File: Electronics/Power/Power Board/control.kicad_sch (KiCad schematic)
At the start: 10 parts, among them IC1 STM32U575VGT6, IC2 TJA1057GT/3, J2 USB4056-03-A, J4 Screw_Terminal_01x02, J5 TC2030

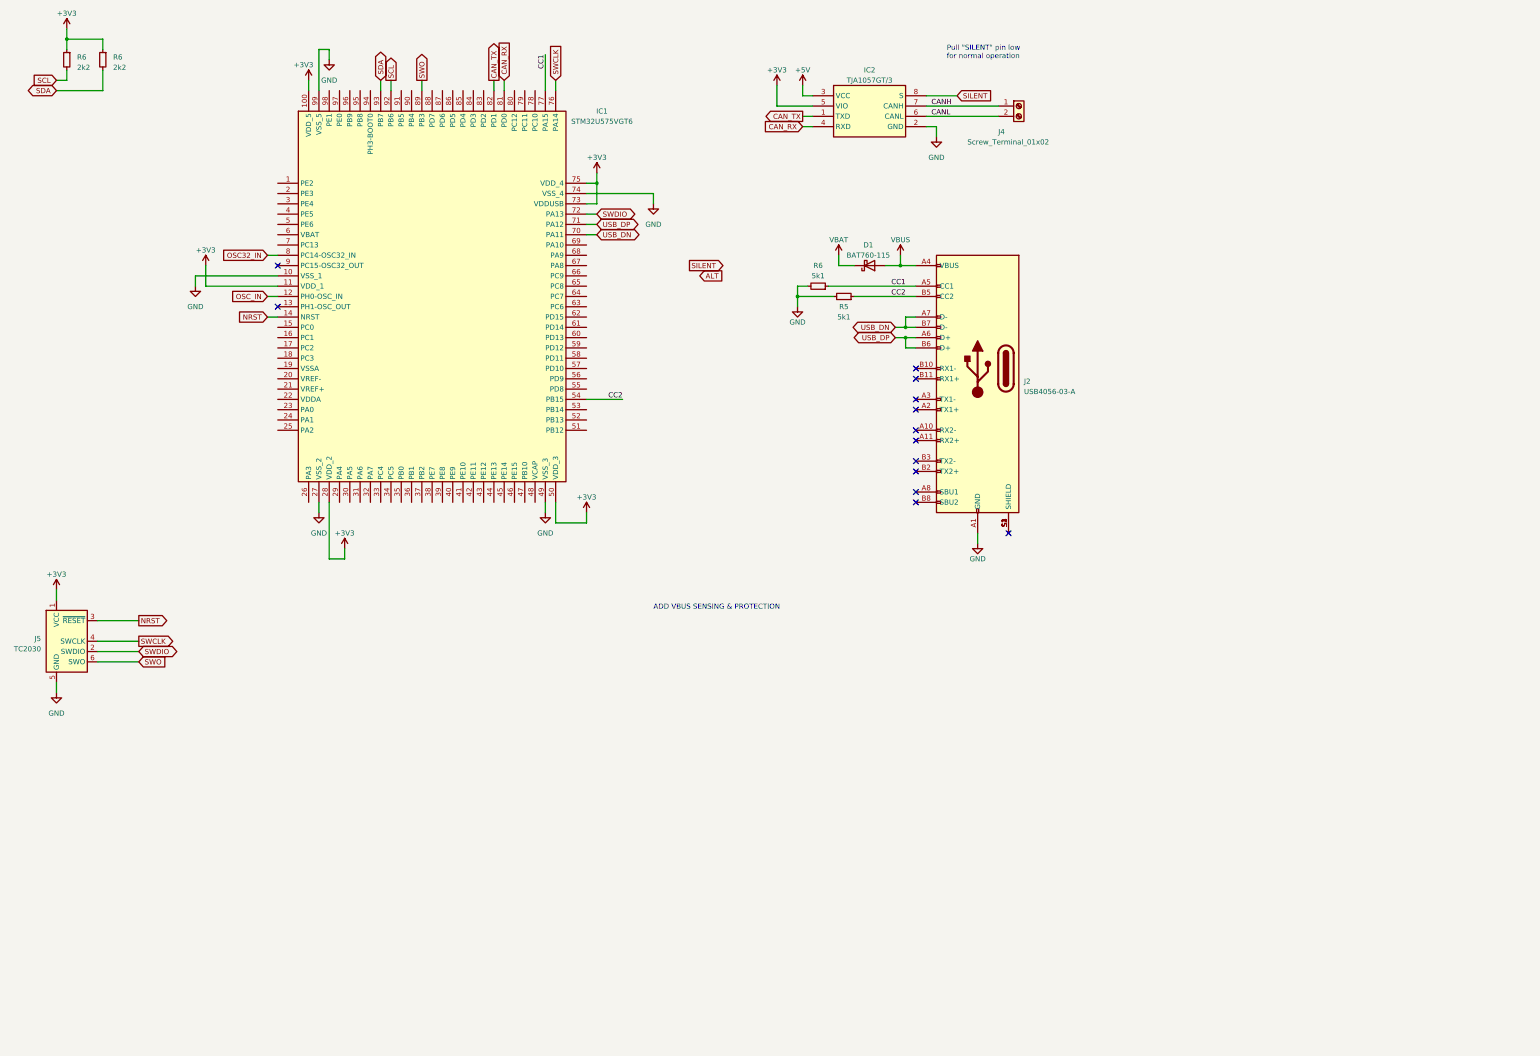
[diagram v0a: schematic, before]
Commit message: Motor driver + power board progress
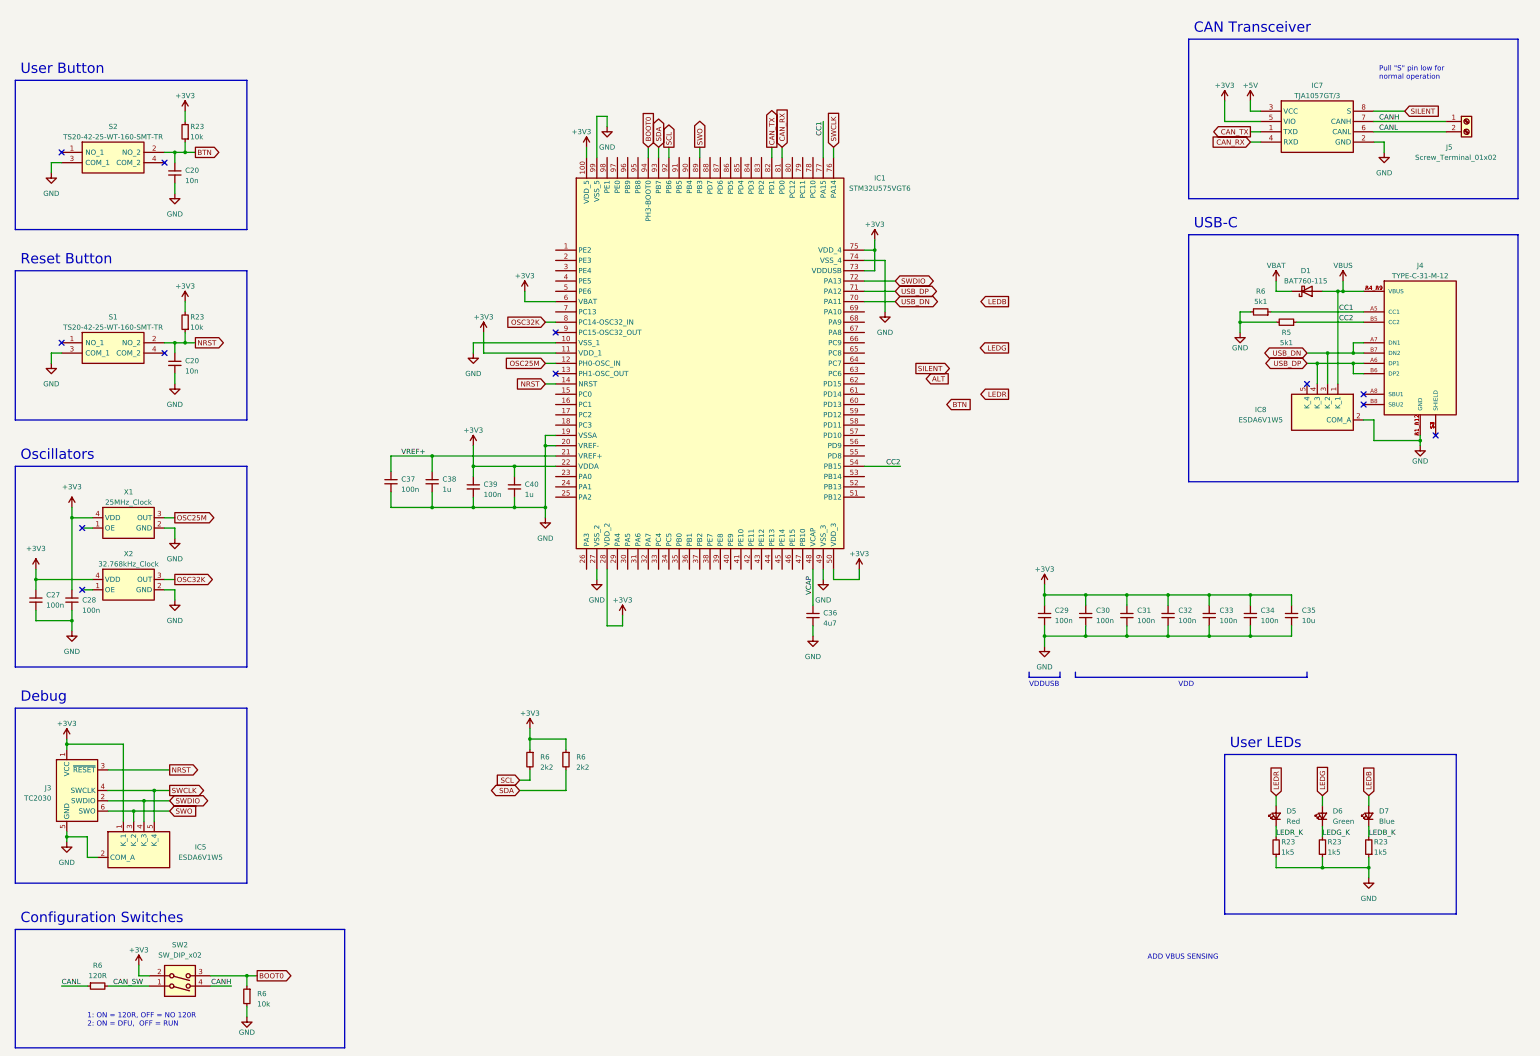
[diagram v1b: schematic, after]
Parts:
- removed J2: USB4056-03-A, MSL Footprints:USB405603A, symbol USB4056-03-A-MSL:USB4056-03-A
- added C20 (x2): 10n, Capacitor_SMD:C_0402_1005Metric, symbol Device:C_Small
- added C27, C28, C29, C30, C31, C32, C33, C34, C37, C39: 100n, Capacitor_SMD:C_0402_1005Metric, symbol Device:C_Small
- added C35: 10u, Capacitor_SMD:C_0402_1005Metric, symbol Device:C_Small
- added C36: 4u7, Capacitor_SMD:C_0402_1005Metric, symbol Device:C_Small
- added C38, C40: 1u, Capacitor_SMD:C_0402_1005Metric, symbol Device:C_Small
- added D5: Red, LED_SMD:LED_0603_1608Metric, symbol Device:LED_Small
- added D6: Green, LED_SMD:LED_0603_1608Metric, symbol Device:LED_Small
- added D7: Blue, LED_SMD:LED_0603_1608Metric, symbol Device:LED_Small
- added IC5, IC8: ESDA6V1W5, SOT65P210X110-5N, symbol ESDA6V1W5:ESDA6V1W5
- added J4: TYPE-C-31-M-12, MSL Footprints:HRO_TYPE-C-31-M-12, symbol TYPE-C-31-M-12:TYPE-C-31-M-12
- added R23 (x2), R6: 10k, Resistor_SMD:R_0402_1005Metric, symbol Device:R_Small
- added R23 (x3): 1k5, Resistor_SMD:R_0402_1005Metric, symbol Device:R_Small
- added R6: 120R, Resistor_SMD:R_0402_1005Metric, symbol Device:R_Small
- added S1, S2: TS20-42-25-WT-160-SMT-TR, MSL Footprints:TS204225WT160SMTTRMSL, symbol TS20-42-25-WT-160-SMT-TR-MSL:TS20-42-25-WT-160-SMT-TR
- added SW2: SW_DIP_x02, Package_DIP:DIP-4_W8.89mm_SMDSocket_LongPads, symbol Switch:SW_DIP_x02
- added X1: 25MHz_Clock, Oscillator:Oscillator_SMD_Abracon_ASE-4Pin_3.2x2.5mm_HandSoldering, symbol MSL_Symbols:25MHz_Clock
- added X2: 32.768kHz_Clock, Oscillator:Oscillator_SMD_Abracon_ASE-4Pin_3.2x2.5mm_HandSoldering, symbol MSL_Symbols:32.768kHz_Clock
- renumbered IC2 to IC7, J5 to J3, J4 to J5
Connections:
- net +3V3: now also IC1.22 (VDDA), IC1.6 (VBAT), C27.1, C28.2, C29.1, C30.1, C31.1, C32.1, C33.1, C34.1, C35.1, C39.1, C40.1, IC5.1 (K_1), R23.2, R23.2, SW2.2, X1.4 (VDD), X2.4 (VDD)
- net CANH: now also SW2.4
- net CANL: now also R6.1
- net CC1: now also J4.A5 (CC1)
- net CC2: now also J4.B5 (CC2)
- net GND: now also IC1.19 (VSSA), IC1.20 (VREF-), C20.2, C20.2, C27.2, C28.1, C29.2, C30.2, C31.2, C32.2, C33.2, C34.2, C35.2, C36.2, C37.2, C38.2, C39.2, C40.2, IC5.2 (COM_A), IC8.2 (COM_A), J4.A1_B12 (GND), J4.B1_A12 (GND), R23.1, R23.1, R23.1, R6.2, S1.3 (COM_1), S2.3 (COM_1), X1.2 (GND), X2.2 (GND)
- net NRST: now also C20.1, R23.1, S1.2 (NO_2)
- net SWCLK: now also IC5.5 (K_4)
- net SWDIO: now also IC5.4 (K_3)
- net SWO: now also IC5.3 (K_2)
- net USB_DN: now also IC8.3 (K_2), J4.A7 (DN1), J4.B7 (DN2)
- net USB_DP: now also IC8.4 (K_3), J4.A6 (DP1), J4.B6 (DP2)
- net VBUS: now also IC8.1 (K_1), J4.A4_B9 (VBUS), J4.B4_A9 (VBUS)
- net VREF+: now reaches IC1.21 (VREF+)
- net VREF+: now also C37.1, C38.1
- net VCAP: now reaches IC1.48 (VCAP)
- net VCAP: now also C36.1
- net BOOT0: now reaches IC1.94 (PH3-BOOT0)
- net BOOT0: now also R6.1, SW2.3
- net OSC32_IN renamed OSC32K
- net OSC32K: now also X2.3 (OUT)
- net OSC_IN renamed OSC25M
- net OSC25M: now also X1.3 (OUT)
- new net: J4.S1 (SHIELD), J4.S2 (SHIELD), J4.S3 (SHIELD), J4.S4 (SHIELD)
- new net BTN: C20.1, R23.1, S2.2 (NO_2)
- new net CAN_SW: R6.2, SW2.1
- new net LEDB: D7.2 (A)
- new net LEDB_K: D7.1 (K), R23.2
- new net LEDG: D6.2 (A)
- new net LEDG_K: D6.1 (K), R23.2
- new net LEDR: D5.2 (A)
- new net LEDR_K: D5.1 (K), R23.2
- no-connect marks 13 -> 12
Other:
- note added: "1: ON = 120R, OFF = NO 120R 2: ON = DFU, OFF = RUN"
- note added: "ADD VBUS SENSING"
- note added: "CAN Transceiver"
- note added: "Configuration Switches"
- note added: "Debug"
- note added: "Oscillators"
- note added: "Pull "S" pin low for normal operation"
- note added: "Reset Button"
- note added: "USB-C"
- note added: "User Button"
- note added: "User LEDs"
- note added: "VDD"
- note added: "VDDUSB"
- note removed: "ADD VBUS SENSING & PROTECTION"
- note removed: "Pull "SILENT" pin low for normal operation"
- moved on the sheet: D1, IC1, IC7, J3, J5, R5, R6

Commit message: PCB Schematic progress
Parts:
- removed IC5, IC8: ESDA6V1W5, SOT65P210X110-5N, symbol ESDA6V1W5:ESDA6V1W5
- removed J4: TYPE-C-31-M-12, MSL Footprints:HRO_TYPE-C-31-M-12, symbol TYPE-C-31-M-12:TYPE-C-31-M-12
- added J1: TYPE-C-31-M-12, MSL Footprints:HRO_TYPE-C-31-M-12, symbol TYPE-C-31-M-12:TYPE-C-31-M-12
- added U1, U2: USBLC6-4SC6-ES, Package_TO_SOT_SMD:SOT-23-6, symbol MSL_Symbols:USBLC6-4SC6-ES
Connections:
- net +3V3: now also U2.5 (VBUS)
- net CC1: now also J1.A5 (CC1), U1.1 (IO1)
- net CC2: now also J1.B5 (CC2), U1.3 (IO2)
- net GND: now also J1.A1_B12 (GND), J1.B1_A12 (GND), U1.2 (GND), U2.2 (GND)
- net NRST: now also U2.6 (IO4)
- net SWCLK: now also U2.4 (IO3)
- net SWDIO: now also U2.3 (IO2)
- net SWO: now also U2.1 (IO1)
- net USB_DN: now also J1.A7 (DN1), J1.B7 (DN2), U1.6 (IO4)
- net USB_DP: now also J1.A6 (DP1), J1.B6 (DP2), U1.4 (IO3)
- net VBUS: now also J1.A4_B9 (VBUS), J1.B4_A9 (VBUS), U1.5 (VBUS)
- net VBAT renamed VIN
- new net: J1.S1 (SHIELD), J1.S2 (SHIELD), J1.S3 (SHIELD), J1.S4 (SHIELD)
- no-connect marks 12 -> 11
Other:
- note added: "Decoupling Capacitors"
- note added: "I2C Pullups"
- moved on the sheet: C29, C30, C31, C32, C33, C34, C35, C36, C37, C38, C39, C40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

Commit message: PCB Schematics finished
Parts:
- renumbered C27 to C301, C28 to C302, C37 to C305, C38 to C306, C39 to C307, C40 to C308, C36 to C309, C29 to C310, C30 to C311, C31 to C312, C32 to C313, C33 to C314, C34 to C315, C35 to C316, IC7 to IC302, J5 to J303, S2 to S301, S1 to S302, SW2 to SW301, X1 to X301, X2 to X302
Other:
- moved on the sheet: R6

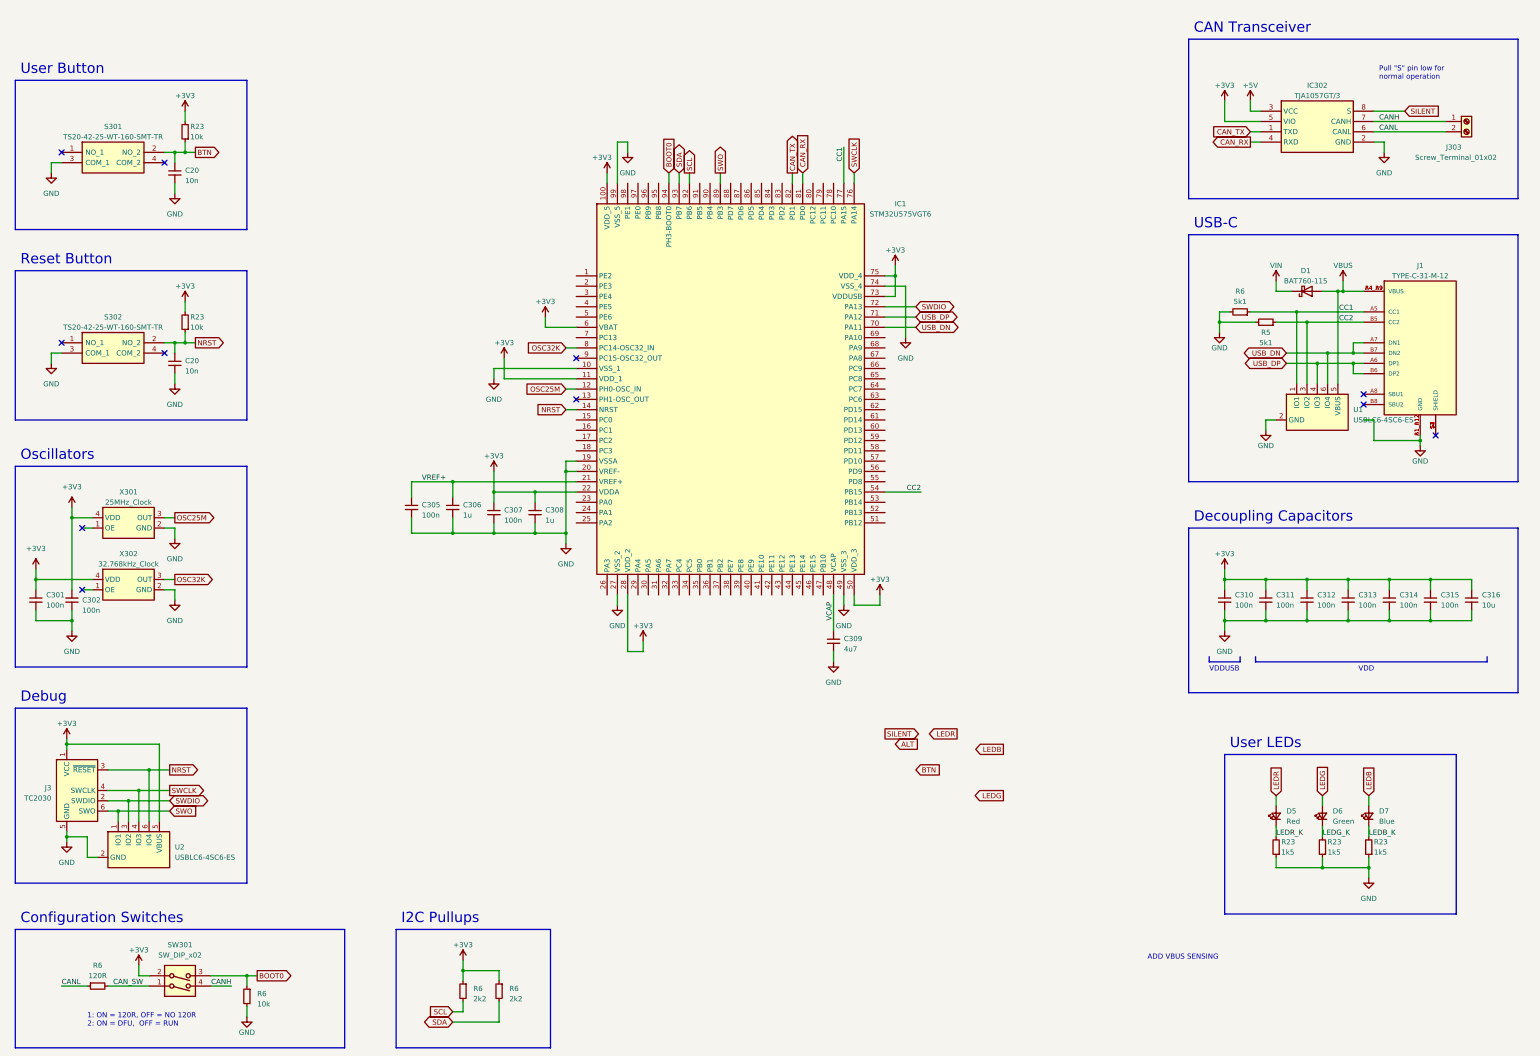
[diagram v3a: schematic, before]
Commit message: Schematic updates
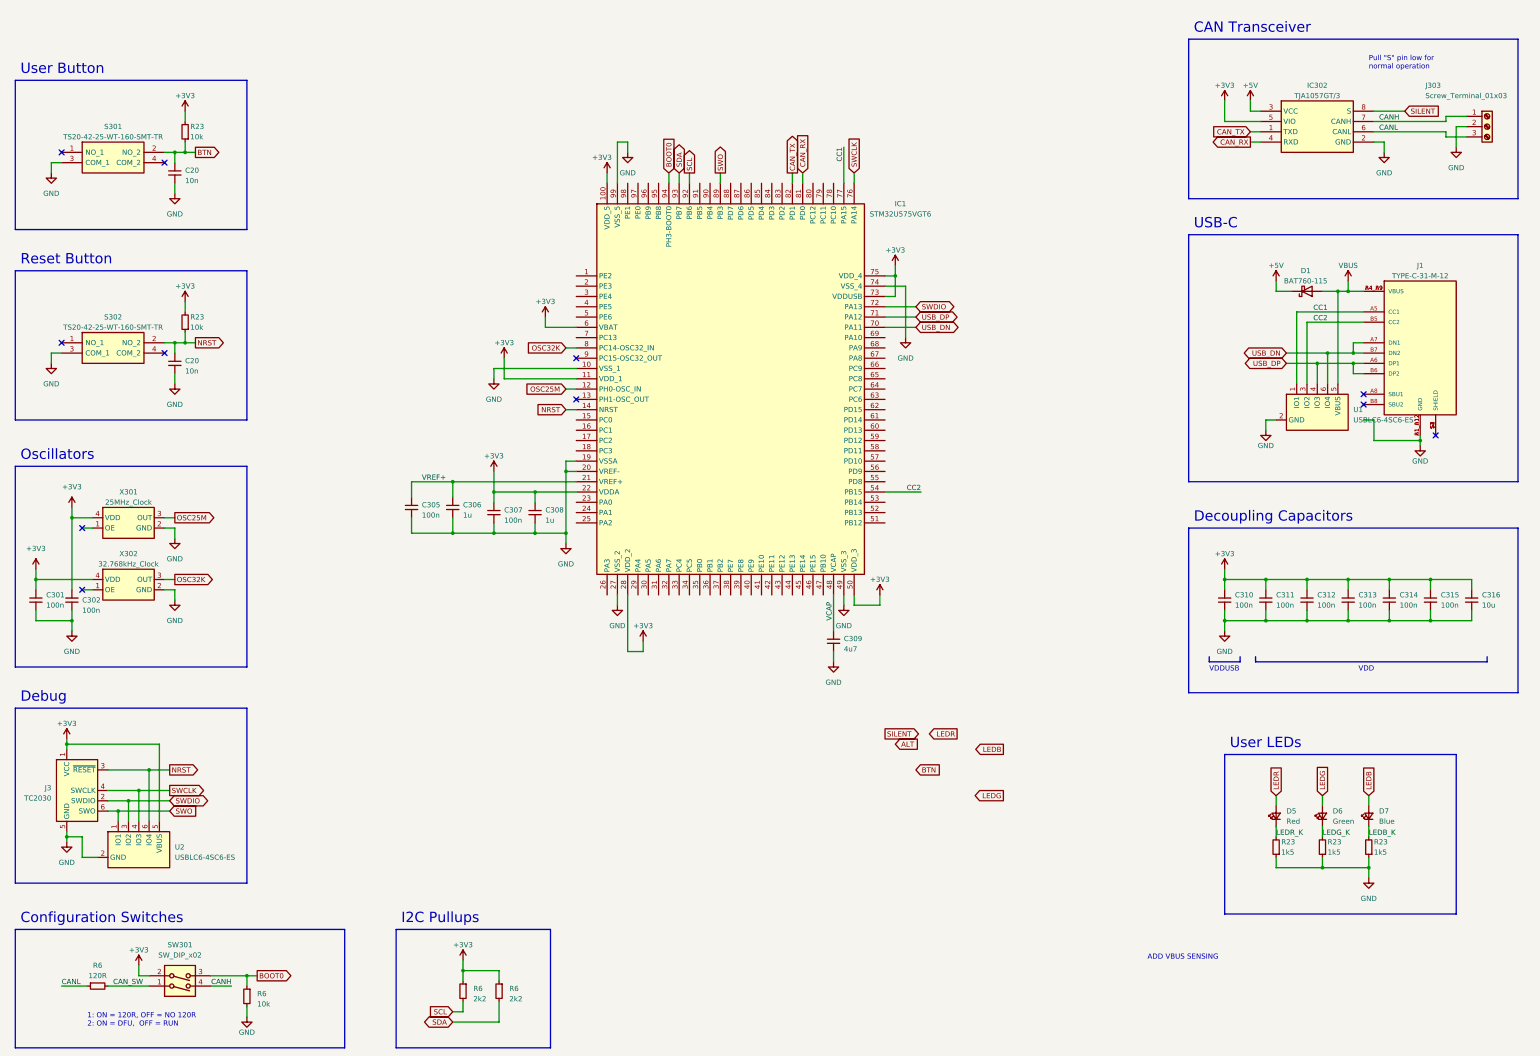
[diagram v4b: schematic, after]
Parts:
- removed J303: Screw_Terminal_01x02, TerminalBlock:TerminalBlock_bornier-2_P5.08mm, symbol Connector:Screw_Terminal_01x02
- removed R5, R6: 5k1, Resistor_SMD:R_0402_1005Metric, symbol Device:R_Small
- added J303: Screw_Terminal_01x03, TerminalBlock:TerminalBlock_bornier-3_P5.08mm, symbol Connector:Screw_Terminal_01x03
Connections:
- net VIN is gone; now on net +5V: D1.1 (K)
- net CANH: now also J303.1 (Pin_1)
- net CANL: now also J303.3 (Pin_3)
- net GND: now also J303.2 (Pin_2)

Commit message: PCB layout progress, spice simulations for power board
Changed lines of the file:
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@@
+    )
+  )
+  (global_label "12V_EN" (shape output) (at 256.54 193.04 180) (fields_autoplaced)
+    (effects (font (size 1.27 1.27)) (justify right))
+    (property "Intersheetrefs" "${INTERSHEET_REFS}" (at 246.6795 193.04 0)
+      (effects (font (size 1.27 1.27)) (justify right) hide)
     )
   )

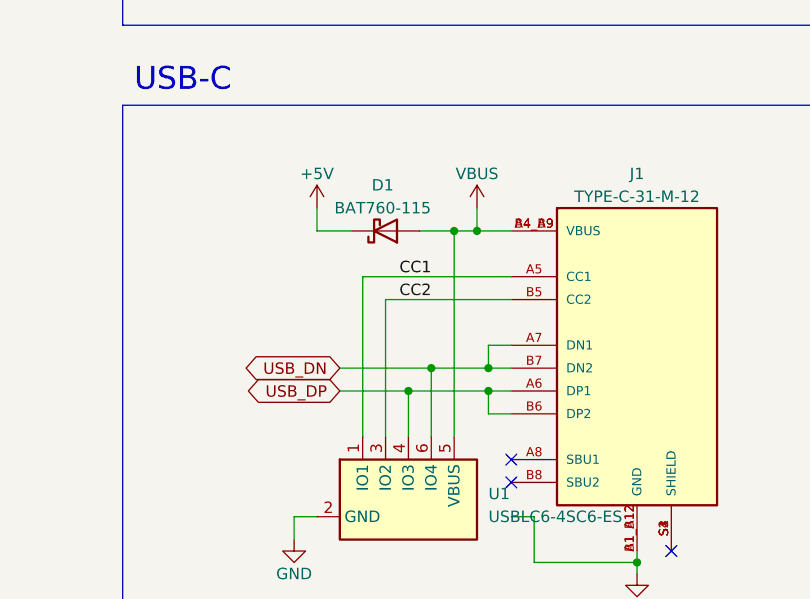
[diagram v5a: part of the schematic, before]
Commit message: Implemented power supply selector
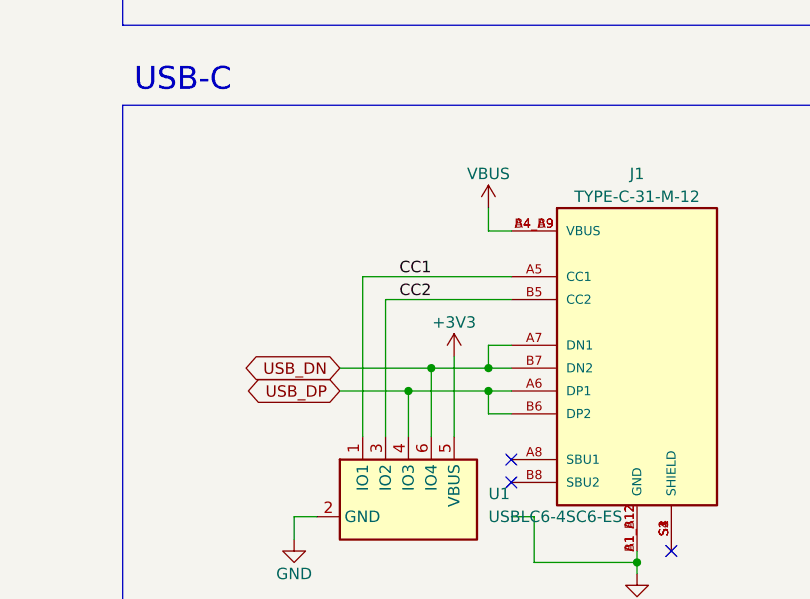
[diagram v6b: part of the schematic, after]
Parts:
- removed D1: BAT760-115, Diode_SMD:D_SOD-323, symbol Device:D_Schottky
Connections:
- net +3V3: now also U1.5 (VBUS)
- net VBUS: no longer U1.5 (VBUS)

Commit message: Finished power board layout
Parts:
- added R6 (x2): 10k, Resistor_SMD:R_0402_1005Metric, symbol Device:R_Small
- added R6 (x2): 1k, Resistor_SMD:R_0402_1005Metric, symbol Device:R_Small
- added U303: TVS1800DRV, Package_SON:WSON-6-1EP_2x2mm_P0.65mm_EP1x1.6mm, symbol Power_Protection:TVS1800DRV
- U2: now not fitted; now left out of the parts list
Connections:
- net GND: now also R6.2, R6.2, U303.1 (GND), U303.2 (GND), U303.3 (GND), U303.7 (GND)
- net SCL: now also IC1.52 (PB13); no longer IC1.92 (PB6)
- net SDA: now also IC1.53 (PB14); no longer IC1.93 (PB7)
- net VBUS: now also R6.1, U303.4 (IN), U303.5 (IN), U303.6 (IN)
- new net VBAT: R6.1
- new net VBAT/11: R6.1, R6.2
- new net VBUS/11: R6.1, R6.2
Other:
- note removed: "ADD VBUS SENSING"
